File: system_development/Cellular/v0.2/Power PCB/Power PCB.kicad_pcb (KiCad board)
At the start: 2 copper layers, 30.5 x 53.3 mm, 15 parts, among them J1 Barrel_Jack, SW1 SW_DIP_x01, SW2 SW_DIP_x01, U1 LF15_TO252, U2 INA219A

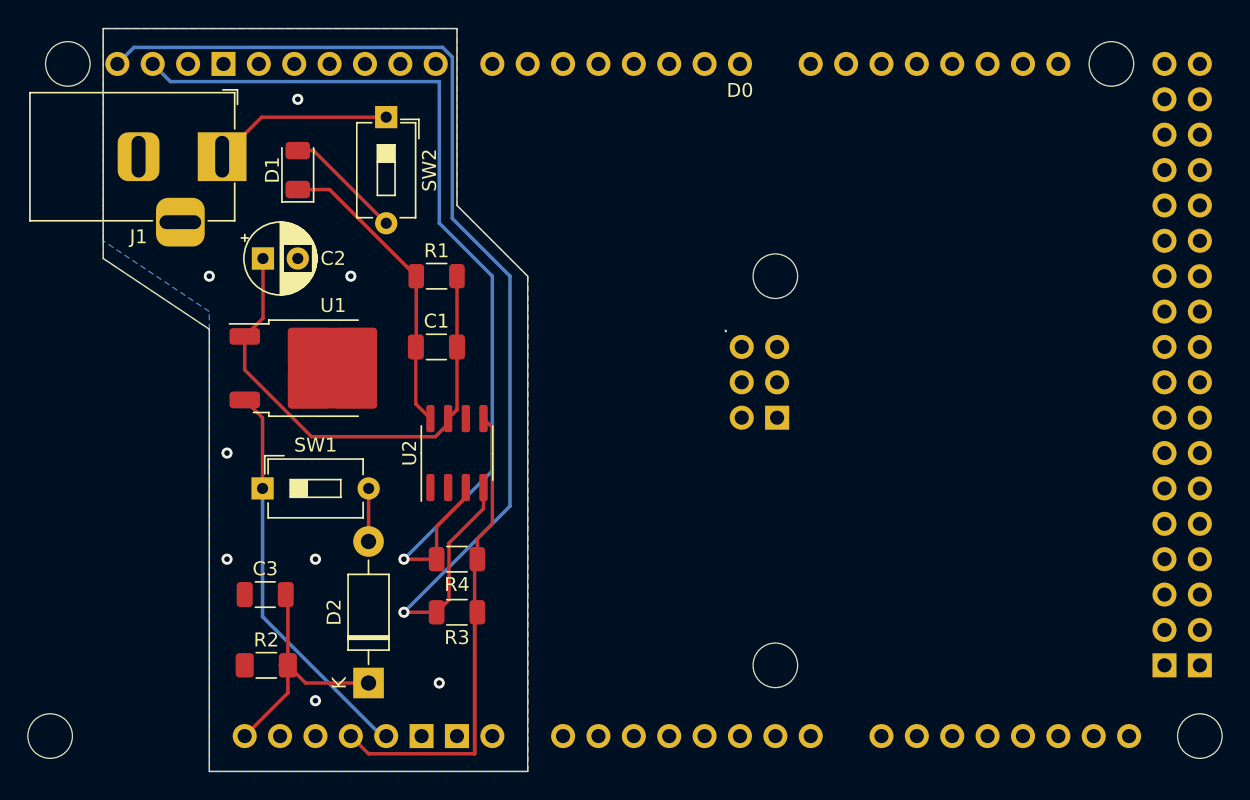
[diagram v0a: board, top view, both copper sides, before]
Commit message: Redid Power PCB
Needed to redo Power PCB for accurate parts sizes
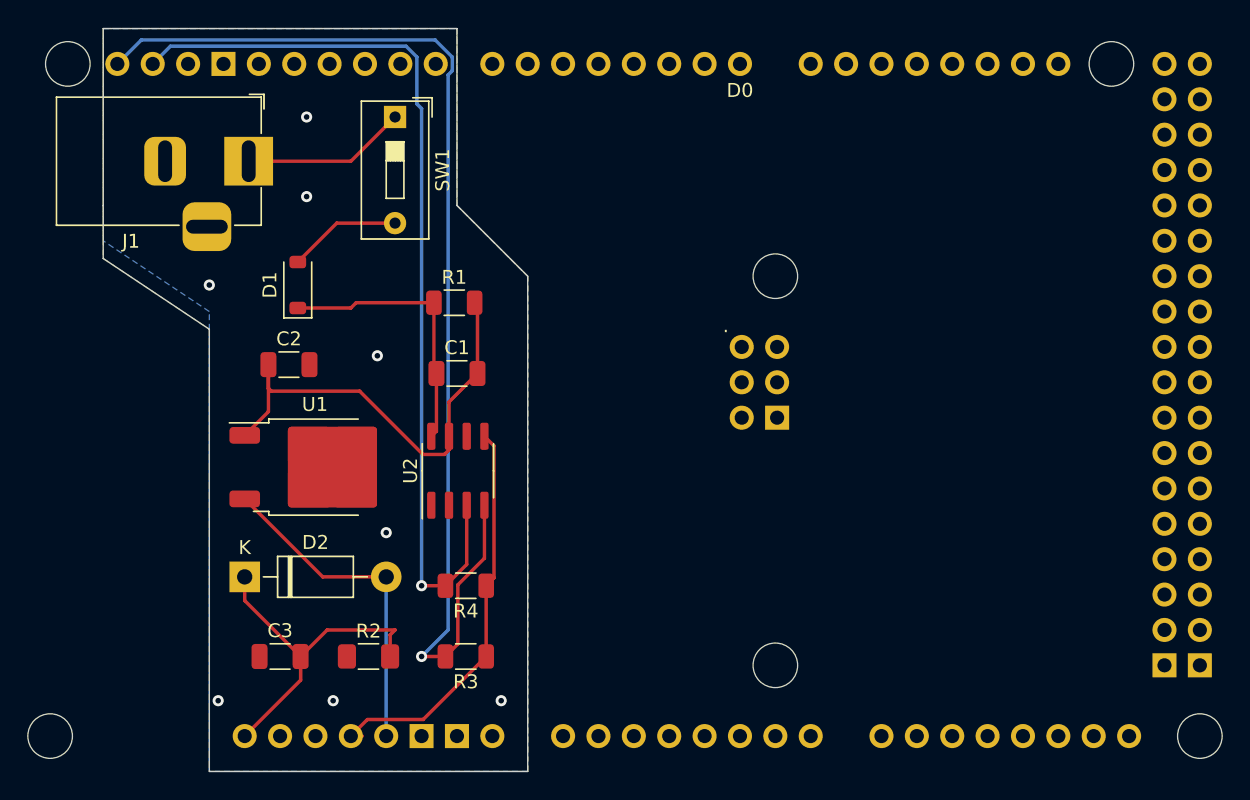
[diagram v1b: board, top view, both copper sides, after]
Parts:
- removed SW2: SW_DIP_x01, Button_Switch_THT:SW_DIP_SPSTx01_Slide_6.7x4.1mm_W7.62mm_P2.54mm_LowProfile
- C2: value C -> 0.1 μF; footprint Capacitor_THT:CP_Radial_D5.0mm_P2.50mm -> Capacitor_SMD:C_1206_3216Metric
- D1: footprint Diode_SMD:D_1206_3216Metric -> Diode_SMD:D_SOD-123
- SW1: footprint Button_Switch_THT:SW_DIP_SPSTx01_Slide_6.7x4.1mm_W7.62mm_P2.54mm_LowProfile -> Button_Switch_THT:SW_DIP_SPSTx01_Slide_9.78x4.72mm_W7.62mm_P2.54mm
- moved SW1 28.3 mm to (137.8, 64.8), turned to -90 degrees
- moved D2 11.7 mm to (127.0, 97.8), turned to 0 degrees
- moved D1 8.25 mm to (130.8, 76.8)
- moved C2 7.84 mm to (130.2, 82.5)
- moved R2 7.37 mm to (135.9, 103.5)
- moved U1 7.10 mm to (132.0, 89.9)
- moved C3 4.57 mm to (129.5, 103.5)
- moved R3 3.24 mm to (142.9, 103.5)
- moved C1 2.41 mm to (142.2, 83.2)
- moved R1 2.29 mm to (142.0, 78.1)
- moved R4 2.01 mm to (142.9, 98.4)
- moved J1 1.93 mm to (127.3, 67.9)
- moved U2 1.27 mm to (142.3, 90.2)
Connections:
- SW1 pad 1: Net-(U1-VO) -> Net-(J1-Pad1)
- SW1 pad 2: Net-(D2-A) -> Net-(D1-A)
- U1 pad 3: Net-(U1-VO) -> Net-(D2-A)
- XA1 pad 5V1: Net-(U1-VO) -> Net-(D2-A)
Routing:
- net Net-(U1-VO): track 28.5 -> 0.00 mm
- net Net-(D2-A): track 3.81 -> 23.9 mm
- net Net-(U2-VS): track 44.8 -> 29.2 mm
- net Net-(D2-K): track 18.4 -> 24.4 mm
- net Net-(U1-VI): track 36.4 -> 34.1 mm
- net Net-(D1-K): track 21.7 -> 19.7 mm
- net Net-(U2-SDA): track 68.0 -> 66.0 mm
- net Net-(J1-Pad1): track 13.0 -> 11.8 mm
- net Net-(U2-SCL): track 82.3 -> 83.0 mm
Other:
- outline, holes or cut-outs redrawn
- board text added: "Nicholas Liger 06/18/24 ARTS Lab - USC Power Board v0.21"
- board text removed: "Power Board v1.0 5/10/2024 Nicholas Liger ARTS Lab - USC"
